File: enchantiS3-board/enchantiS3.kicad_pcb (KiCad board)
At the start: 4 copper layers, 55.9 x 25.4 mm, 54 parts, among them J1 USB_C_Receptacle_USB2.0, SW1 BOOT, SW2 ESP_RST, SW3 SYS_RST, U1 USBLC6-2P6, U2 NCP187, U3 ICM-42670-P, U7 NPM1300-QEAA-R7, U8 MMC5983MA

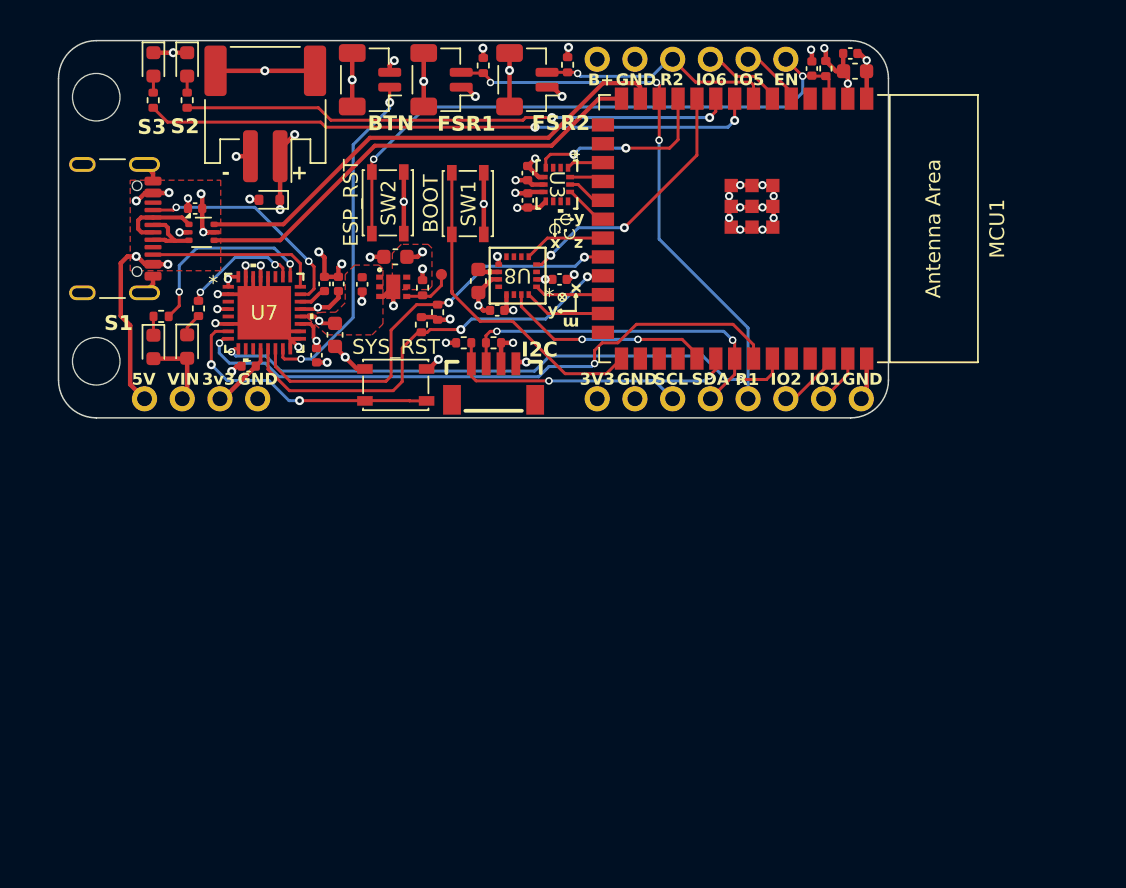
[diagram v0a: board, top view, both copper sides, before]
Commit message: Moved all subschematics to a folder
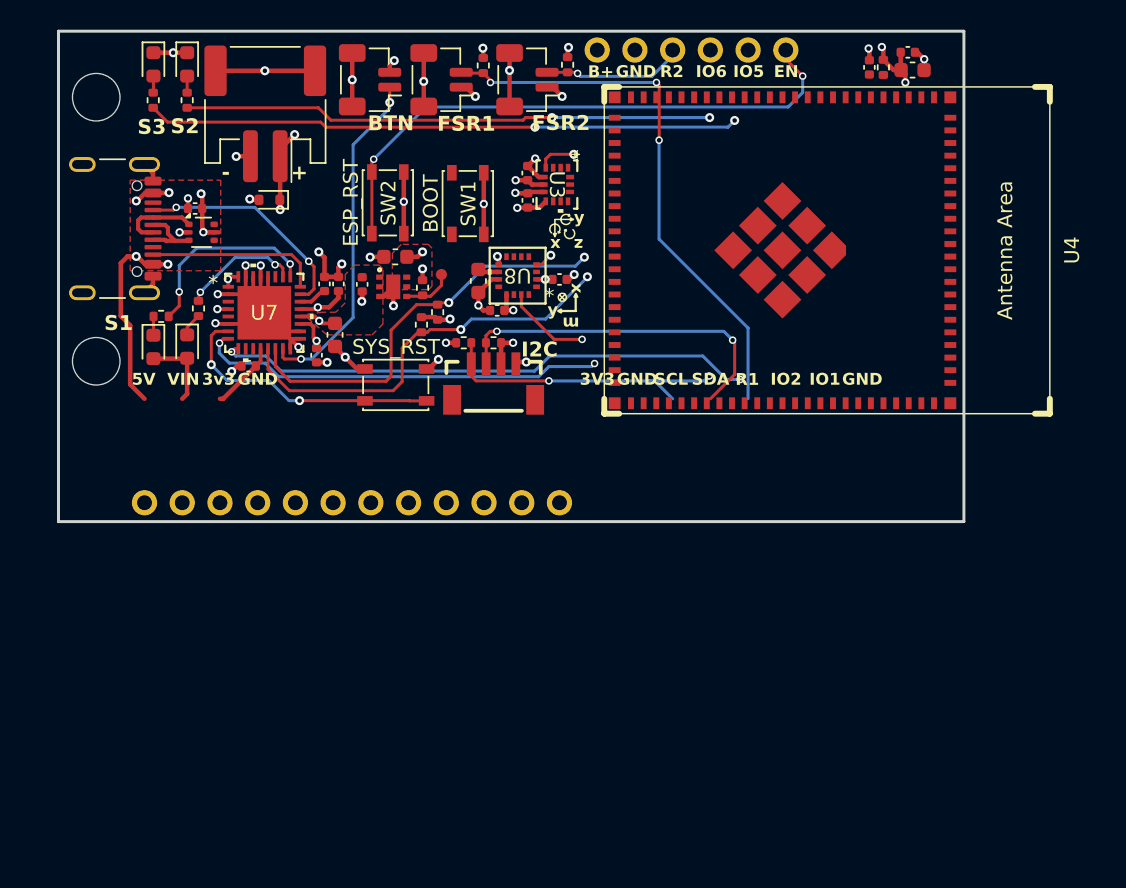
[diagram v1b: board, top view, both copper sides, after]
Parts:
- removed MCU1: ESP32-S3-WROOM-1, PCM_Espressif:ESP32-S3-WROOM-1
- added U4: ~, Espressif:ESP32-S31-WROOM-3, F.Cu at (141.5, 62.4)
- BOARDLAYOUT1: footprint ENCHANTI_enchanti-board-symbols:enchantiS3-layout -> ENCHANTI_enchanti-board-symbols:enchantiC5-layout
- moved BOARDLAYOUT1 14.6 mm to (134.1, 64.1)
- moved C13 3.87 mm to (150.2, 50.2)
- moved C2 3.87 mm to (149.9, 49.0)
- moved C9 3.87 mm to (147.3, 50.1)
- moved R5 3.87 mm to (148.2, 50.1)
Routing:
- net /MCU/USBD-: track 33.5 -> 0.00 mm
- net /MCU/USBD+: track 31.4 -> 0.00 mm
- net /MCU/IO0: track 22.2 -> 0.00 mm
- net GND: track 109.5 -> 88.8 mm, vias 46 -> 36
- net /MCU/MAG_CS: track 17.7 -> 1.22 mm, vias 2 -> 1
- net /MCU/GPIO41: track 41.5 -> 27.7 mm
- net /Motion Sensing/IMU_INT1: track 12.8 -> 2.61 mm, vias 2 -> 1
- net /MCU/MAG_INT: track 14.3 -> 5.81 mm, vias 2 -> 1
- net /MCU/FSR2: track 16.1 -> 9.05 mm
- net /MCU/MAG_COPI: track 5.52 -> 0.00 mm
- net /MCU/MAG_CIPO: track 5.51 -> 0.00 mm
- net /MCU/IO6: track 5.45 -> 0.00 mm
- net /MCU/MAG_SCLK: track 4.69 -> 0.00 mm
- net /MCU/IO5: track 4.26 -> 0.00 mm
- net /MCU/IO2: track 4.25 -> 0.00 mm
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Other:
- board size 55.9 x 25.4 mm -> 61 x 33 mm

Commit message: Added circuit for magnetometer, added circuit for canfd transceiver, updated circuit for USB connector
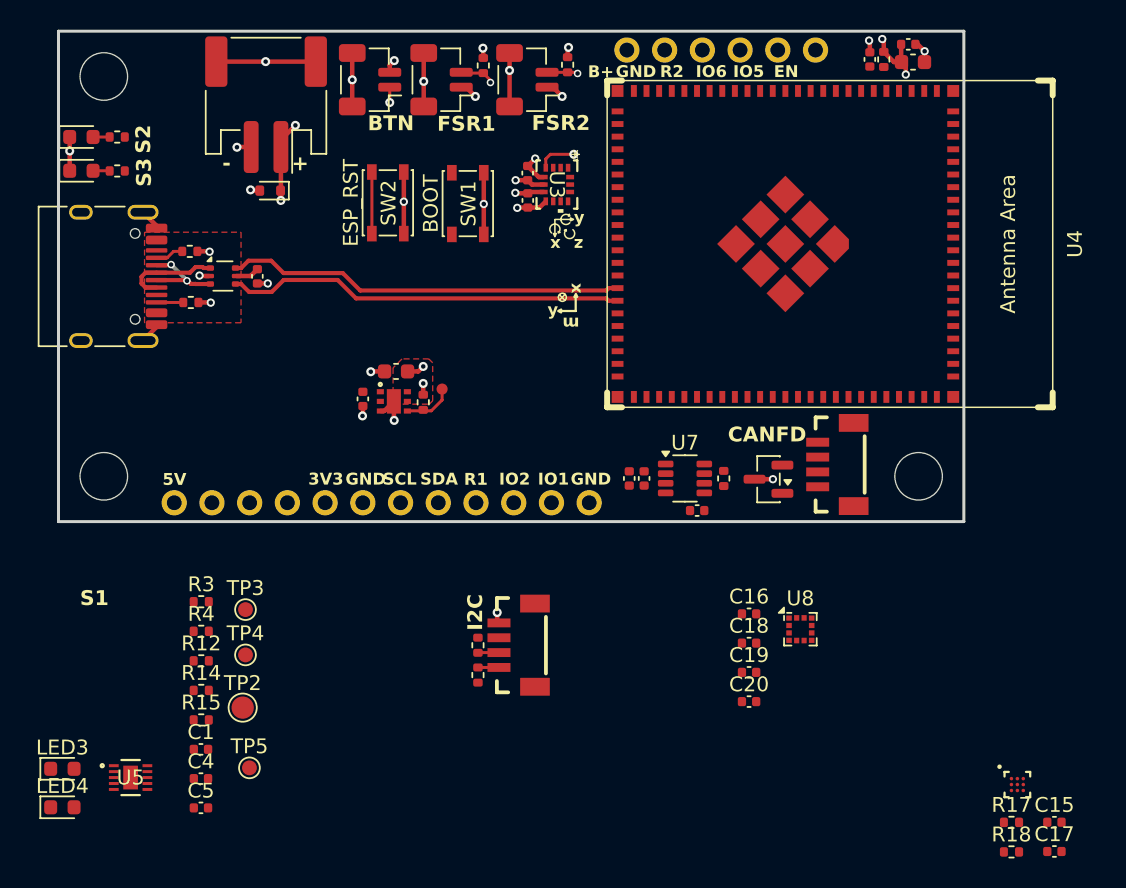
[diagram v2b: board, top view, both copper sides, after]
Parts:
- removed CHARGLED4: RED_LED, LED_SMD:LED_0603_1608Metric
- removed CHARGLED5: YELLOW_LED, LED_SMD:LED_0603_1608Metric
- removed SW3: SYS_RST, ENCHANTI_switches:SW_SPST_PTS810
- added C12: 0.1uF, Capacitor_SMD:C_0402_1005Metric, F.Cu at (106.1, 64.1)
- added C14: 0.1uF, Capacitor_SMD:C_0402_1005Metric, F.Cu at (135.7, 79.9)
- added C16: 1uF, Capacitor_SMD:C_0402_1005Metric, F.Cu at (139.2, 86.9)
- added C17: 0.47uF, Capacitor_SMD:C_0402_1005Metric, F.Cu at (159.8, 102.9)
- added D2: NUP2105L, Package_TO_SOT_SMD:SOT-23, F.Cu at (140.5, 77.8)
- added H3: MountingHole, MountingHole:MountingHole_3.2mm_M3_DIN965, F.Cu at (150.6, 77.6)
- added LED3: Yellow, LED_SMD:LED_0603_1608Metric, F.Cu at (93.0, 97.3)
- added LED4: Red, LED_SMD:LED_0603_1608Metric, F.Cu at (93.0, 99.9)
- added R11: 5K1, Resistor_SMD:R_0402_1005Metric, F.Cu at (101.5, 62.5)
- added R13: 5K1, Resistor_SMD:R_0402_1005Metric, F.Cu at (101.6, 65.9)
- added R14: 0.43k, Resistor_SMD:R_0402_1005Metric, F.Cu at (102.3, 92.0)
- added R15: 10k, Resistor_SMD:R_0402_1005Metric, F.Cu at (102.3, 94.0)
- added R16: 120, Resistor_SMD:R_0402_1005Metric, F.Cu at (137.5, 77.7)
- added R17: 2k2, Resistor_SMD:R_0402_1005Metric, F.Cu at (156.9, 100.9)
- added TOUCH2: JST-SH-1x04 1.0mm, ENCHANTI_connectors:JST_SMD_1.0mm-4_Vertical, F.Cu at (145.3, 76.8)
- added TP2: TestPoint, TestPoint:TestPoint_Pad_D1.5mm, F.Cu at (105.1, 93.2)
- added TP3: TestPoint, TestPoint:TestPoint_Pad_D1.0mm, F.Cu at (105.3, 86.6)
- added TP4: TestPoint, TestPoint:TestPoint_Pad_D1.0mm, F.Cu at (105.3, 89.6)
- added TP5: TestPoint, TestPoint:TestPoint_Pad_D1.0mm, F.Cu at (105.6, 97.2)
- added U5: BQ25185DLHR, ENCHANTI_battery-management:WSON10_DLH_TEX, F.Cu at (97.6, 97.9)
- added U6: MAX17262REWL+T, ENCHANTI_battery-management:MAX17262, F.Cu at (157.3, 98.3)
- C18: value 2.2uF -> 0.1uF
- C19: value 10uF -> 0.1uF; footprint Capacitor_SMD:C_0603_1608Metric -> Capacitor_SMD:C_0402_1005Metric
- C4: value 1uF -> 10uF
- C5: value 10uF -> 1uF; footprint Capacitor_SMD:C_0603_1608Metric -> Capacitor_SMD:C_0402_1005Metric
- J1: footprint Connector_USB:USB_C_Receptacle_GCT_USB4105-xx-A_16P_TopMnt_Horizontal -> Connector_USB:USB_C_Receptacle_HRO_TYPE-C-31-M-12
- R12: value 2k -> 13k
- R18: value 2k -> 2k2
- R3, R4: value 2k2 -> 2k
- U7: value NPM1300-QEAA-R7 -> TCAN3413DDFR; footprint ENCHANTI_battery-management:QFN32_5X5_NOR -> ENCHANTI_transceivers:TSOT-23-8_DDF_TEX
- U8: value MMC5983MA -> LIS3MDL; footprint ENCHANTI_MEMS:MMC5983MA_MEM -> Package_LGA:LGA-12_2x2mm_P0.5mm
- moved C15 71.1 mm to (159.8, 100.9), turned to 0 degrees
- moved R18 65.8 mm to (156.9, 102.9), turned to 0 degrees
- moved C20 40.6 mm to (139.2, 92.8), turned to 0 degrees
- moved C18 35.0 mm to (139.2, 88.8), turned to 0 degrees
- moved C4 34.3 mm to (102.3, 98.0), turned to 0 degrees
- moved C5 33.1 mm to (102.3, 99.9), turned to 0 degrees
- moved C1 32.7 mm to (102.3, 96.0), turned to 0 degrees
- moved C19 32.0 mm to (139.2, 90.8), turned to 0 degrees
- moved U8 30.5 mm to (142.7, 87.9), turned to 0 degrees
- moved U7 30.4 mm to (134.9, 77.7)
- moved R4 26.7 mm to (102.3, 88.0), turned to 0 degrees
- moved R3 23.8 mm to (102.3, 86.0), turned to 0 degrees
- moved R12 23.3 mm to (102.3, 90.0)
- moved R7 22.4 mm to (121.0, 91.0), turned to -90 degrees
- moved R9 20.4 mm to (121.0, 89.0), turned to 90 degrees
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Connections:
- net /MCU/GPIO41 renamed /Peripherals/STB
- C15 pad 1: VUSB -> +BATT
- C18 pad 1: +BATT -> +3V3
- C19 pad 1: Net-(U8-CAP) -> +3V3
- C20 pad 1: +3V3 -> Net-(U8-C1)
- C4 pad 1: /Power System/VBUSOUT -> SYS
- C5 pad 1: SYS -> CHRG+
- C6 pad 1: +3V3 -> /Peripherals/VCC
- C7 pad 1: +3V3 -> /Peripherals/VCC
- J1 pad A5: /Power System/CC1 -> /USB/CC1
- J1 pad B5: /Power System/CC2 -> /USB/CC2
- R12 pad 1: Net-(CHARGLED4-K) -> /Power System/VSET
- R12 pad 2: /Power System/LED0 -> GND
- R18 pad 1: Net-(CHARGLED5-K) -> +3V3
- R18 pad 2: /Power System/LED1 -> /Power System/FG_SCL
- R3 pad 1: /MCU/I2C_SDA_MAIN -> /Power System/LED1
- R3 pad 2: +3V3 -> /Power System/STAT1
- R4 pad 1: /MCU/I2C_SCL_MAIN -> /Power System/LED0
- R4 pad 2: +3V3 -> /Power System/STAT2
- U1 pad 1: /USB/D- -> /USB/D+
- U1 pad 3: /USB/D+ -> /USB/D-
- U1 pad 4: /MCU/USBD+ -> /MCU/USBD-
- U1 pad 6: /MCU/USBD- -> /MCU/USBD+
- U7 pad 1: SYS -> /Peripherals/TXD
- U7 pad 3: unconnected-(U7-SW1-Pad3) -> /Peripherals/VCC
- U7 pad 4: SYS -> /Peripherals/RXD
- U7 pad 5: unconnected-(U7-SW2-Pad5) -> /Peripherals/VIO
- U7 pad 6: GND -> /Peripherals/CAN_L
- U7 pad 7: /Power System/RESET -> /Peripherals/CAN_H
- U8 pad 10: Net-(U8-CAP) -> /MCU/MAG_CS
- U8 pad 11: GND -> /MCU/MAG_COPI
- U8 pad 12: unconnected-(U8-NC-Pad12) -> GND
- U8 pad 2: +3V3 -> GND
- U8 pad 3: unconnected-(U8-NC-Pad3) -> GND
- U8 pad 4: /MCU/MAG_CS -> Net-(U8-C1)
- U8 pad 5: /MCU/MAG_CIPO -> +3V3
- U8 pad 6: unconnected-(U8-NC-Pad6) -> +3V3
- U8 pad 7: unconnected-(U8-NC-Pad7) -> /Motion Sensing/MAG_INT
- U8 pad 8: unconnected-(U8-NC-Pad8) -> /Motion Sensing/MAG_DRDY
- U8 pad 9: GND -> /MCU/MAG_CIPO
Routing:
- net /MCU/BLUELED: track 39.9 -> 0.00 mm, vias 2 -> 0
- net GND: track 88.8 -> 50.4 mm, vias 36 -> 25
- net +3V3: track 50.0 -> 13.2 mm, vias 13 -> 8
- net +BATT: track 42.9 -> 6.47 mm, vias 3 -> 2
- net /MCU/GPIO42: track 36.4 -> 0.00 mm, vias 2 -> 0
- net /MCU/ORANGELED: track 35.6 -> 0.00 mm, vias 2 -> 0
- net /MCU/FSR1: track 37.4 -> 2.34 mm, vias 3 -> 1
- net /MCU/EN: track 38.5 -> 4.15 mm, vias 2 -> 0
- net VUSB: track 33.0 -> 1.59 mm, vias 7 -> 0
- net /MCU/I2C_SDA_MAIN: track 28.0 -> 0.00 mm, vias 2 -> 0
- net /MCU/I2C_SCL_MAIN: track 27.9 -> 0.00 mm, vias 2 -> 0
- net /Peripherals/STB: track 27.7 -> 0.00 mm, vias 2 -> 0
- net /MCU/USBD-: track 0.00 -> 26.9 mm
- net /MCU/USBD+: track 0.00 -> 26.8 mm
- net SYS: track 26.2 -> 0.00 mm, vias 3 -> 0
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- removed copper zone on F.Cu, net SYS
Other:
- board text added: "CANFD"
- board text added: "EnchantiS31 v0.4 2024-10 Albert Niyonsenga"
- board text removed: "3v3"
- board text removed: "EnchantiS3 v0.4 2024-10 Albert Niyonsenga"
- board text removed: "VIN"

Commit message: Added can transceiver circuit, finished routing power traces
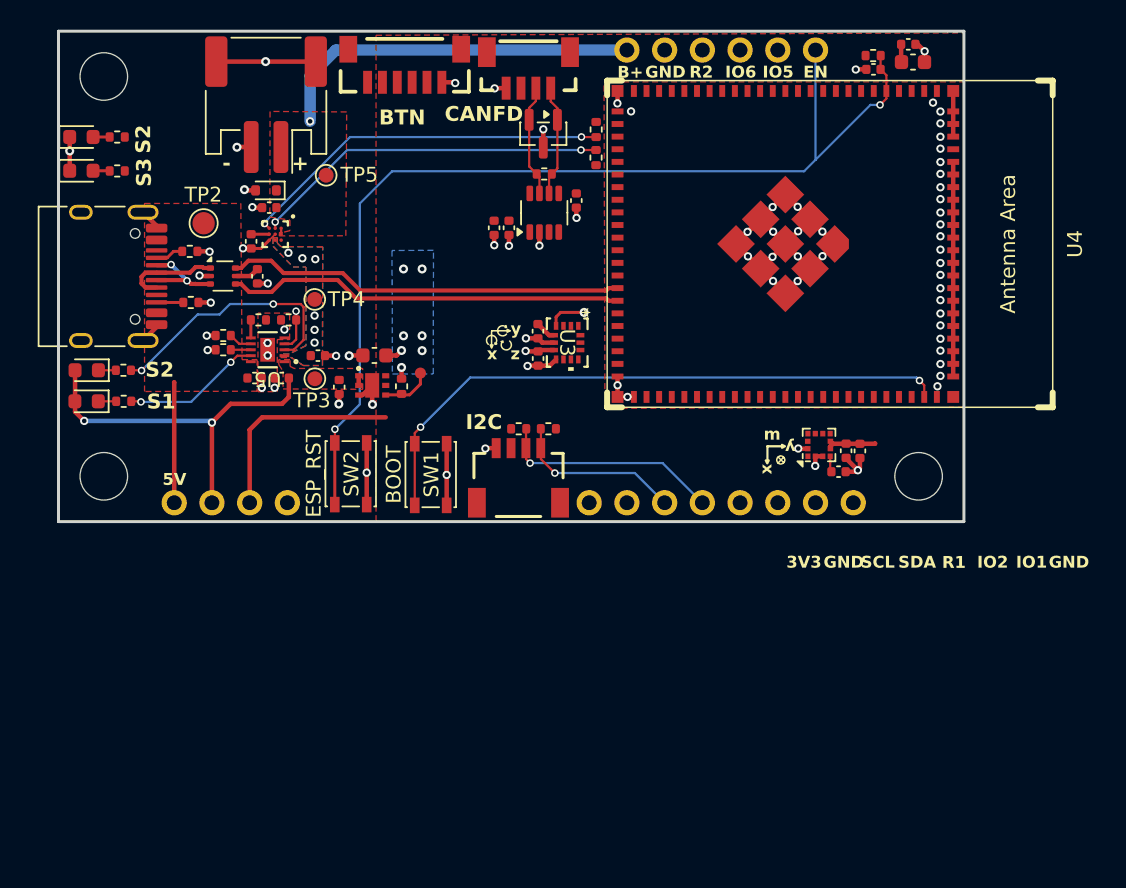
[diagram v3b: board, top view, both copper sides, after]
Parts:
- removed ANG1, ANG2, ANG3: CONN HEADER SMD 2POS 1MM, ENCHANTI_connectors:Molex_Pico-Clasp_2pin_Vertical
- removed C18: 0.1uF, Capacitor_SMD:C_0402_1005Metric
- removed R1, R2: 1k, Resistor_SMD:R_0402_1005Metric
- removed TOUCH1: JST-SH-1x04 1.0mm, ENCHANTI_connectors:JST_SMD_1.0mm-4_Vertical
- added J2: Conn_01x06, PCM_SparkFun-Connector:JST_1x06_P1.0mm_Vertical_SMD, F.Cu at (116.0, 49.8)
- added J3: Qwiic_Connector, PCM_SparkFun-Connector:JST_1x04_P1.0mm_Horizontal_SMD, F.Cu at (123.7, 75.7)
- added R19: 10k, Resistor_SMD:R_0402_1005Metric, F.Cu at (108.2, 67.1)
- BOARDLAYOUT1: footprint ENCHANTI_enchanti-board-symbols:enchantiC5-layout -> ENCHANTI_enchanti-board-symbols:enchantis31-layout
- moved C17 67.9 mm to (105.7, 61.8), turned to -90 degrees
- moved C15 67.1 mm to (106.9, 59.5), turned to 180 degrees
- moved U6 62.2 mm to (107.3, 61.3), turned to -90 degrees
- moved R18 54.5 mm to (128.9, 56.1), turned to 90 degrees
- moved R17 54.4 mm to (128.9, 54.2), turned to -90 degrees
- moved TP5 40.2 mm to (110.7, 57.3)
- moved TOUCH2 34.1 mm to (124.3, 50.0), turned to 0 degrees
- moved TP2 32.7 mm to (102.5, 60.6), turned to 180 degrees
- moved C5 31.5 mm to (110.2, 69.5)
- moved U5 30.2 mm to (106.8, 69.1), turned to 180 degrees
- moved LED4 29.5 mm to (94.6, 70.5), turned to 180 degrees
- moved D2 27.8 mm to (125.3, 54.5), turned to -90 degrees
- moved C4 27.5 mm to (107.7, 71.0), turned to 180 degrees
- moved R15 27.2 mm to (106.2, 67.1), turned to 180 degrees
- moved C1 25.3 mm to (105.9, 71.0)
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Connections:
- net Net-(U8-C1) renamed /Motion Sensing/C1
- C14 pad 1: /Peripherals/VIO -> +3V3
- C6 pad 1: /Peripherals/VCC -> +3V3
- C7 pad 1: /Peripherals/VCC -> +3V3
- SW1 pad 1: /MCU/IO0 -> /MCU/BOOT
- U4 pad 71: unconnected-(U4-GPIO61-Pad71) -> /MCU/BOOT
- U5 pad 4: GND -> /Power System/~{CE}
- U6 pad B2: /Power System/FG_ALRT -> GND
- U7 pad 3: /Peripherals/VCC -> +3V3
- U7 pad 5: /Peripherals/VIO -> +3V3
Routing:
- net /MCU/EN: track 4.15 -> 69.8 mm, vias 0 -> 2
- net GND: track 50.4 -> 102.5 mm, vias 25 -> 78
- net /MCU/BOOT: track 0.00 -> 41.7 mm, vias 0 -> 2
- net SYS: track 0.00 -> 25.5 mm, vias 0 -> 2
- net /Power System/FG_SDA: track 0.00 -> 25.2 mm, vias 0 -> 2
- net /Power System/FG_SCL: track 0.00 -> 24.0 mm, vias 0 -> 2
- net +BATT: track 6.47 -> 25.5 mm, vias 2 -> 1
- net /Power System/STAT2: track 0.00 -> 17.3 mm, vias 0 -> 2
- net /Peripherals/SDA2: track 1.42 -> 15.4 mm, vias 0 -> 1
- net +3V3: track 13.2 -> 24.6 mm
- net /Peripherals/SCL2: track 1.42 -> 11.8 mm, vias 0 -> 1
- net /Power System/STAT1: track 0.00 -> 9.35 mm, vias 0 -> 2
- net VUSB: track 1.59 -> 9.70 mm
- net /Peripherals/CAN_H: track 0.00 -> 7.56 mm
- net /Peripherals/CAN_L: track 0.00 -> 7.51 mm
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- added copper zone on B.Cu, net +3V3
- added copper zone on F.Cu, net +BATT
- added copper zone on B.Cu, net CHRG+
- added copper zone on F.Cu, net CHRG+
- added copper zone on F.Cu, net GND
- added copper zone on F.Cu, net SYS
- removed copper zone on In2.Cu, net +3V3
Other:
- board text removed: "FSR1"
- board text removed: "FSR1 IO8"
- board text removed: "FSR2"
- board text removed: "FSR2 IO7"
